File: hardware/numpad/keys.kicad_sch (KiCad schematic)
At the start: 30 parts, among them SW10 5, SW12 2, SW13 dot, SW14 times, SW15 9, SW16 6, SW17 3, SW18 minus, SW19 plus, SW2 Num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

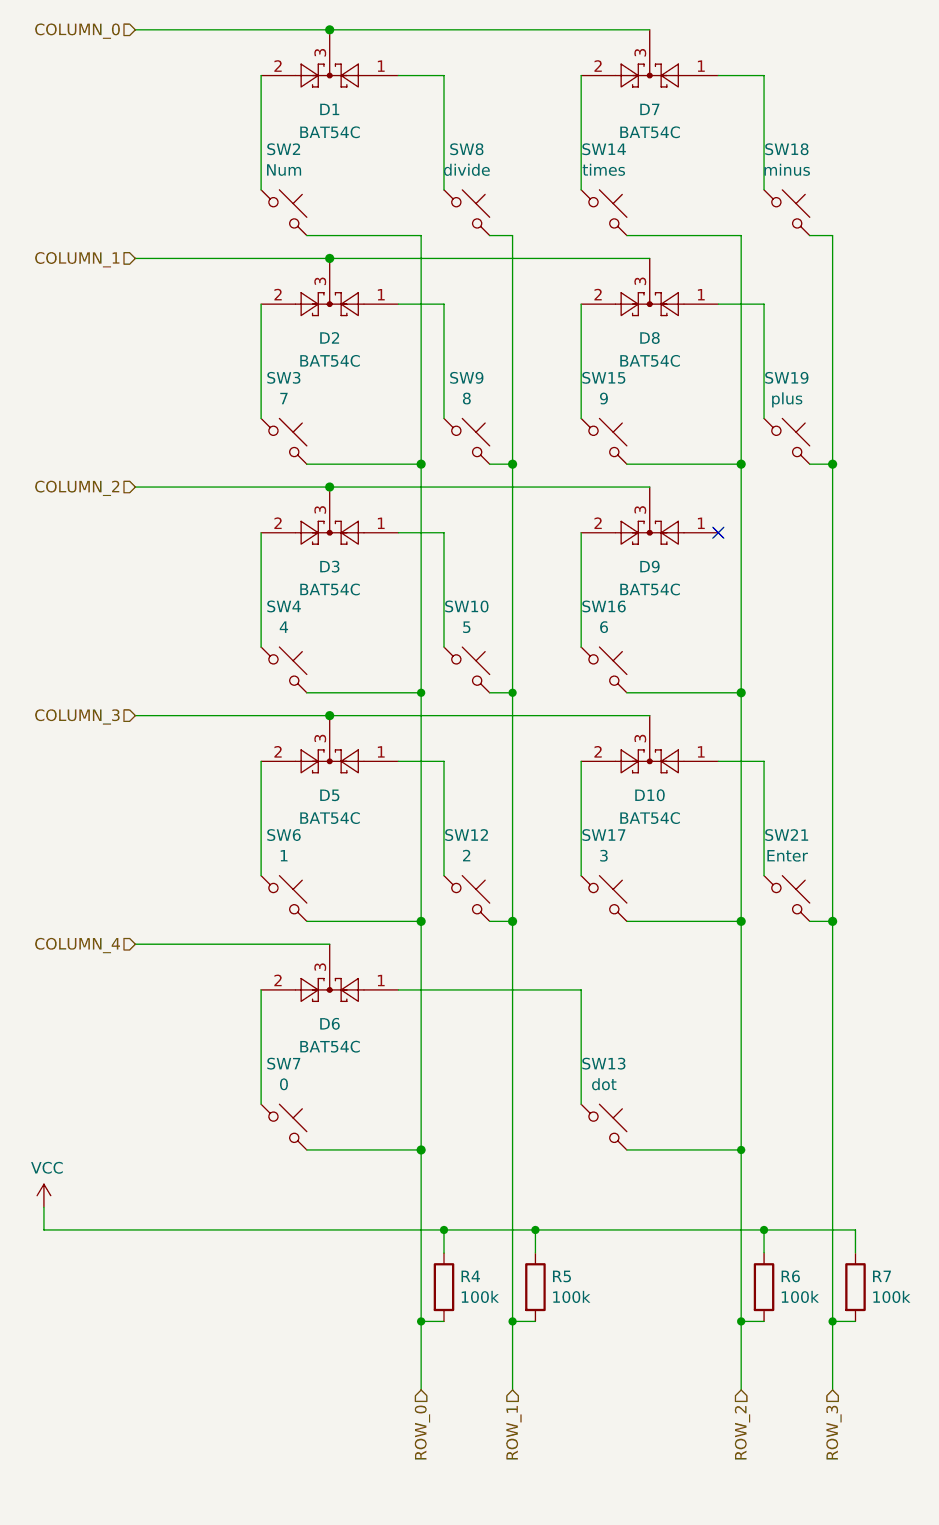
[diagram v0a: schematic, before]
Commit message: Numpad: Fix labels of columns and rows of the key matrix
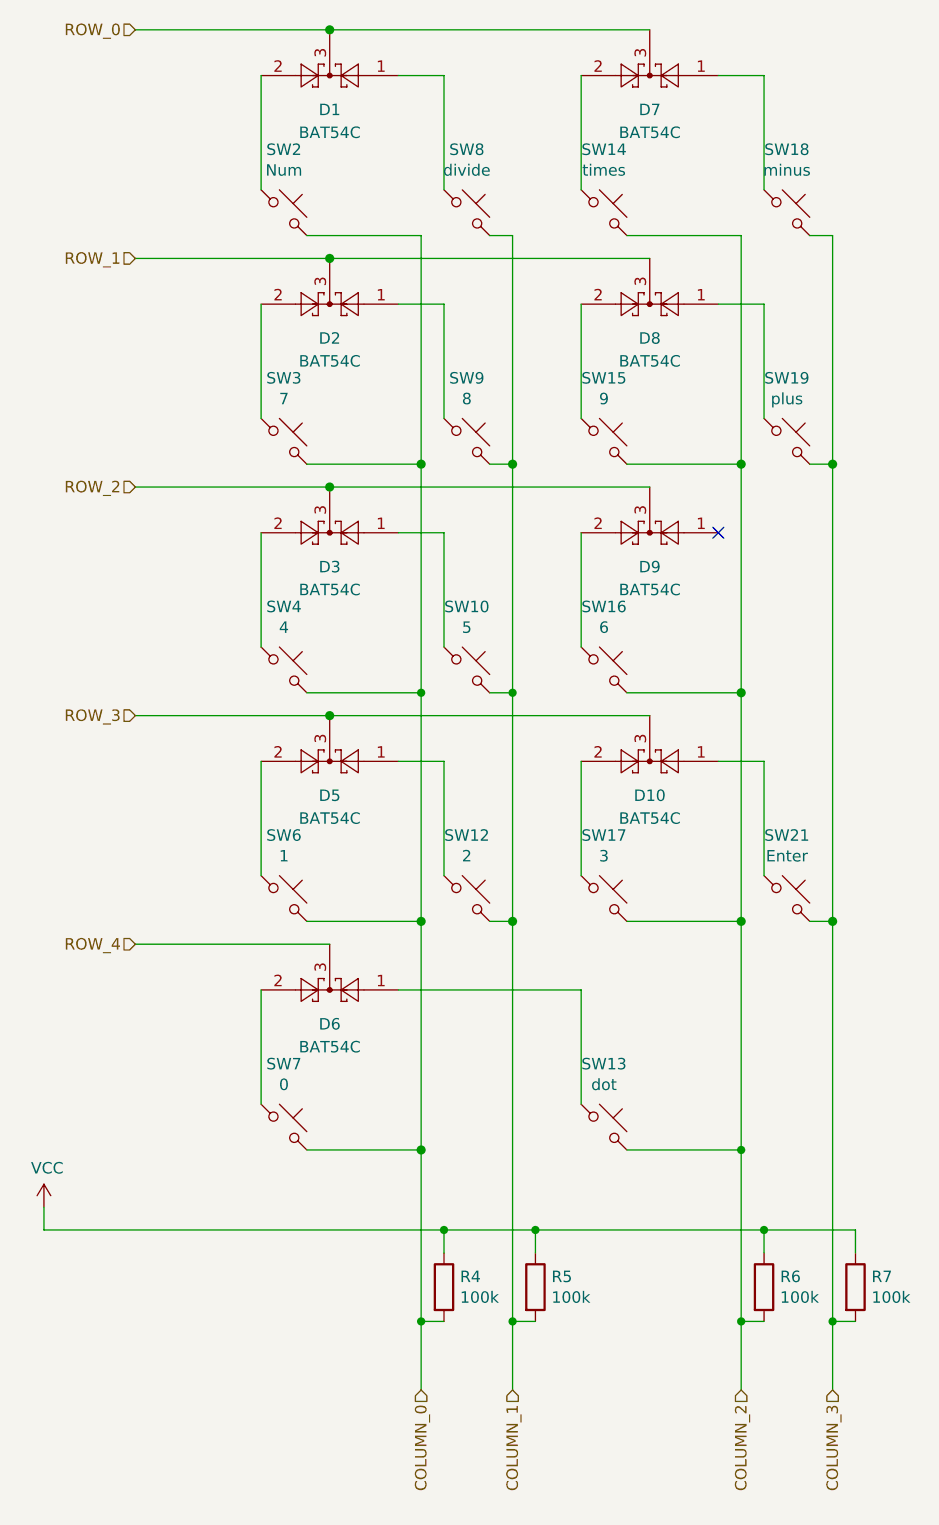
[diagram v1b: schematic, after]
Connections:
- net COLUMN_0: now also R4.2, SW2.2, SW3.2, SW4.2, SW6.2, SW7.2; no longer D1.3, D7.3
- net COLUMN_1: now also R5.2, SW10.2, SW12.2, SW8.2, SW9.2; no longer D2.3, D8.3
- net COLUMN_2: now also R6.2, SW13.2, SW14.2, SW15.2, SW16.2, SW17.2; no longer D3.3, D9.3
- net COLUMN_3: now also R7.2, SW18.2, SW19.2, SW21.2; no longer D10.3, D5.3
- net ROW_0: now also D1.3, D7.3; no longer R4.2, SW2.2, SW3.2, SW4.2, SW6.2, SW7.2
- net ROW_1: now also D2.3, D8.3; no longer R5.2, SW10.2, SW12.2, SW8.2, SW9.2
- net ROW_2: now also D3.3, D9.3; no longer R6.2, SW13.2, SW14.2, SW15.2, SW16.2, SW17.2
- net ROW_3: now also D10.3, D5.3; no longer R7.2, SW18.2, SW19.2, SW21.2
- net COLUMN_4 renamed ROW_4
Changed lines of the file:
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@@
     (stroke (width 0) (type solid) (color 0 0 0 0))
   )
-  (hierarchical_label "COLUMN_0" (shape input) (at 81.28 27.94 180)
+  (hierarchical_label "ROW_0" (shape input) (at 81.28 27.94 180)
     (effects (font (size 1.27 1.27)) (justify right))
   )
-  (hierarchical_label "COLUMN_1" (shape input) (at 81.28 53.34 180)
+  (hierarchical_label "ROW_1" (shape input) (at 81.28 53.34 180)
     (effects (font (size 1.27 1.27)) (justify right))
   )
-  (hierarchical_label "COLUMN_2" (shape input) (at 81.28 78.74 180)
+  (hierarchical_label "ROW_2" (shape input) (at 81.28 78.74 180)
     (effects (font (size 1.27 1.27)) (justify right))
   )
-  (hierarchical_label "COLUMN_3" (shape input) (at 81.28 104.14 180)
+  (hierarchical_label "ROW_3" (shape input) (at 81.28 104.14 180)
     (effects (font (size 1.27 1.27)) (justify right))
   )
-  (hierarchical_label "COLUMN_4" (shape input) (at 81.28 129.54 180)
+  (hierarchical_label "ROW_4" (shape input) (at 81.28 129.54 180)
     (effects (font (size 1.27 1.27)) (justify right))
   )
-  (hierarchical_label "ROW_0" (shape input) (at 113.03 179.07 270)
+  (hierarchical_label "COLUMN_0" (shape input) (at 113.03 179.07 270)
     (effects (font (size 1.27 1.27)) (justify right))
   )
-  (hierarchical_label "ROW_1" (shape input) (at 123.19 179.07 270)
+  (hierarchical_label "COLUMN_1" (shape input) (at 123.19 179.07 270)
     (effects (font (size 1.27 1.27)) (justify right))
   )
-  (hierarchical_label "ROW_2" (shape input) (at 148.59 179.07 270)
+  (hierarchical_label "COLUMN_2" (shape input) (at 148.59 179.07 270)
     (effects (font (size 1.27 1.27)) (justify right))
   )
-  (hierarchical_label "ROW_3" (shape input) (at 158.75 179.07 270)
+  (hierarchical_label "COLUMN_3" (shape input) (at 158.75 179.07 270)
     (effects (font (size 1.27 1.27)) (justify right))
   )

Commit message: Numpad: Add missing part numbers
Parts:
- SW10, SW12, SW13, SW14, SW15, SW16, SW17, SW18, SW19, SW2, SW21, SW3, SW4, SW6, SW7, SW8, SW9: Mouser (none) -> 540-MX1A-E1NW; Part Name (none) -> MX1A-E1NW
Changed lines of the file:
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@@
+      (effects (font (size 1.27 1.27)) hide)
+    )
+    (property "Mouser" "540-MX1A-E1NW" (id 4) (at 97.79 48.26 0)
+      (effects (font (size 1.27 1.27)) hide)
+    )
+    (property "Part Name" "MX1A-E1NW" (id 5) (at 97.79 48.26 0)
       (effects (font (size 1.27 1.27)) hide)
     )
@@
       (effects (font (size 1.27 1.27)) hide)
     )
+    (property "Mouser" "540-MX1A-E1NW" (id 4) (at 97.79 73.66 0)
+      (effects (font (size 1.27 1.27)) hide)
+    )
+    (property "Part Name" "MX1A-E1NW" (id 5) (at 97.79 73.66 0)
+      (effects (font (size 1.27 1.27)) hide)
+    )
     (pin "1")
     (pin "2")
@@
       (effects (font (size 1.27 1.27)) hide)
     )
+    (property "Mouser" "540-MX1A-E1NW" (id 4) (at 97.79 99.06 0)
+      (effects (font (size 1.27 1.27)) hide)
+    )
+    (property "Part Name" "MX1A-E1NW" (id 5) (at 97.79 99.06 0)
+      (effects (font (size 1.27 1.27)) hide)
+    )
     (pin "1")
     (pin "2")
@@
       (effects (font (size 1.27 1.27)) hide)
     )
+    (property "Mouser" "540-MX1A-E1NW" (id 4) (at 97.79 124.46 0)
+      (effects (font (size 1.27 1.27)) hide)
+    )
+    (property "Part Name" "MX1A-E1NW" (id 5) (at 97.79 124.46 0)
+      (effects (font (size 1.27 1.27)) hide)
+    )
     (pin "1")
     (pin "2")
@@
       (effects (font (size 1.27 1.27)) hide)
     )
+    (property "Mouser" "540-MX1A-E1NW" (id 4) (at 97.79 149.86 0)
+      (effects (font (size 1.27 1.27)) hide)
+    )
+    (property "Part Name" "MX1A-E1NW" (id 5) (at 97.79 149.86 0)
+      (effects (font (size 1.27 1.27)) hide)
+    )
     (pin "1")
     (pin "2")
@@
       (effects (font (size 1.27 1.27)) hide)
     )
+    (property "Mouser" "540-MX1A-E1NW" (id 4) (at 118.11 48.26 0)
+      (effects (font (size 1.27 1.27)) hide)
+    )
+    (property "Part Name" "MX1A-E1NW" (id 5) (at 118.11 48.26 0)
+      (effects (font (size 1.27 1.27)) hide)
+    )
     (pin "1")
     (pin "2")
@@
       (effects (font (size 1.27 1.27)) hide)
     )
+    (property "Mouser" "540-MX1A-E1NW" (id 4) (at 118.11 73.66 0)
+      (effects (font (size 1.27 1.27)) hide)
+    )
+    (property "Part Name" "MX1A-E1NW" (id 5) (at 118.11 73.66 0)
+      (effects (font (size 1.27 1.27)) hide)
+    )
     (pin "1")
     (pin "2")
@@
       (effects (font (size 1.27 1.27)) hide)
     )
+    (property "Mouser" "540-MX1A-E1NW" (id 4) (at 118.11 99.06 0)
+      (effects (font (size 1.27 1.27)) hide)
+    )
+    (property "Part Name" "MX1A-E1NW" (id 5) (at 118.11 99.06 0)
+      (effects (font (size 1.27 1.27)) hide)
+    )
     (pin "1")
     (pin "2")
@@
       (effects (font (size 1.27 1.27)) hide)
     )
+    (property "Mouser" "540-MX1A-E1NW" (id 4) (at 118.11 124.46 0)
+      (effects (font (size 1.27 1.27)) hide)
+    )
+    (property "Part Name" "MX1A-E1NW" (id 5) (at 118.11 124.46 0)
+      (effects (font (size 1.27 1.27)) hide)
+    )
     (pin "1")
     (pin "2")
@@
       (effects (font (size 1.27 1.27)) hide)
     )
+    (property "Mouser" "540-MX1A-E1NW" (id 4) (at 133.35 48.26 0)
+      (effects (font (size 1.27 1.27)) hide)
+    )
+    (property "Part Name" "MX1A-E1NW" (id 5) (at 133.35 48.26 0)
+      (effects (font (size 1.27 1.27)) hide)
+    )
     (pin "1")
     (pin "2")
@@
       (effects (font (size 1.27 1.27)) hide)
     )
+    (property "Mouser" "540-MX1A-E1NW" (id 4) (at 133.35 73.66 0)
+      (effects (font (size 1.27 1.27)) hide)
+    )
+    (property "Part Name" "MX1A-E1NW" (id 5) (at 133.35 73.66 0)
+      (effects (font (size 1.27 1.27)) hide)
+    )
     (pin "1")
     (pin "2")
@@
       (effects (font (size 1.27 1.27)) hide)
     )
+    (property "Mouser" "540-MX1A-E1NW" (id 4) (at 133.35 99.06 0)
+      (effects (font (size 1.27 1.27)) hide)
+    )
+    (property "Part Name" "MX1A-E1NW" (id 5) (at 133.35 99.06 0)
+      (effects (font (size 1.27 1.27)) hide)
+    )
     (pin "1")
     (pin "2")
@@
       (effects (font (size 1.27 1.27)) hide)
     )
+    (property "Mouser" "540-MX1A-E1NW" (id 4) (at 133.35 124.46 0)
+      (effects (font (size 1.27 1.27)) hide)
+    )
+    (property "Part Name" "MX1A-E1NW" (id 5) (at 133.35 124.46 0)
+      (effects (font (size 1.27 1.27)) hide)
+    )
     (pin "1")
     (pin "2")
@@
       (effects (font (size 1.27 1.27)) hide)
     )
+    (property "Mouser" "540-MX1A-E1NW" (id 4) (at 133.35 149.86 0)
+      (effects (font (size 1.27 1.27)) hide)
+    )
+    (property "Part Name" "MX1A-E1NW" (id 5) (at 133.35 149.86 0)
+      (effects (font (size 1.27 1.27)) hide)
+    )
     (pin "1")
     (pin "2")
@@
       (effects (font (size 1.27 1.27)) hide)
     )
+    (property "Mouser" "540-MX1A-E1NW" (id 4) (at 153.67 48.26 0)
+      (effects (font (size 1.27 1.27)) hide)
+    )
+    (property "Part Name" "MX1A-E1NW" (id 5) (at 153.67 48.26 0)
+      (effects (font (size 1.27 1.27)) hide)
+    )
     (pin "1")
     (pin "2")
@@
       (effects (font (size 1.27 1.27)) hide)
     )
+    (property "Mouser" "540-MX1A-E1NW" (id 4) (at 153.67 73.66 0)
+      (effects (font (size 1.27 1.27)) hide)
+    )
+    (property "Part Name" "MX1A-E1NW" (id 5) (at 153.67 73.66 0)
+      (effects (font (size 1.27 1.27)) hide)
+    )
     (pin "1")
     (pin "2")
@@
       (effects (font (size 1.27 1.27)) hide)
     )
+    (property "Mouser" "540-MX1A-E1NW" (id 4) (at 153.67 124.46 0)
+      (effects (font (size 1.27 1.27)) hide)
+    )
+    (property "Part Name" "MX1A-E1NW" (id 5) (at 153.67 124.46 0)
+      (effects (font (size 1.27 1.27)) hide)
+    )

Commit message: Numpad: Add pullup for reset and connect BOOT0 to ground
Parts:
- D1, D10, D2, D3, D5, D6, D7, D8, D9: Mouser 241-BAT54A_R1_00001 -> 241-BAT54A_R1_00001
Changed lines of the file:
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@@
       (effects (font (size 1.27 1.27)) hide)
     )
-    (property "Mouser" " 241-BAT54A_R1_00001 " (id 5) (at 102.87 33.02 0)
+    (property "Mouser" "241-BAT54A_R1_00001 " (id 5) (at 102.87 33.02 0)
       (effects (font (size 1.27 1.27)) hide)
     )
@@
       (effects (font (size 1.27 1.27)) hide)
     )
-    (property "Mouser" " 241-BAT54A_R1_00001 " (id 5) (at 102.87 58.42 0)
+    (property "Mouser" "241-BAT54A_R1_00001 " (id 5) (at 102.87 58.42 0)
       (effects (font (size 1.27 1.27)) hide)
     )
@@
       (effects (font (size 1.27 1.27)) hide)
     )
-    (property "Mouser" " 241-BAT54A_R1_00001 " (id 5) (at 102.87 83.82 0)
+    (property "Mouser" "241-BAT54A_R1_00001 " (id 5) (at 102.87 83.82 0)
       (effects (font (size 1.27 1.27)) hide)
     )
@@
       (effects (font (size 1.27 1.27)) hide)
     )
-    (property "Mouser" " 241-BAT54A_R1_00001 " (id 5) (at 102.87 109.22 0)
+    (property "Mouser" "241-BAT54A_R1_00001 " (id 5) (at 102.87 109.22 0)
       (effects (font (size 1.27 1.27)) hide)
     )
@@
       (effects (font (size 1.27 1.27)) hide)
     )
-    (property "Mouser" " 241-BAT54A_R1_00001 " (id 5) (at 102.87 134.62 0)
+    (property "Mouser" "241-BAT54A_R1_00001 " (id 5) (at 102.87 134.62 0)
       (effects (font (size 1.27 1.27)) hide)
     )
@@
       (effects (font (size 1.27 1.27)) hide)
     )
-    (property "Mouser" " 241-BAT54A_R1_00001 " (id 5) (at 138.43 33.02 0)
+    (property "Mouser" "241-BAT54A_R1_00001 " (id 5) (at 138.43 33.02 0)
       (effects (font (size 1.27 1.27)) hide)
     )
@@
       (effects (font (size 1.27 1.27)) hide)
     )
-    (property "Mouser" " 241-BAT54A_R1_00001 " (id 5) (at 138.43 58.42 0)
+    (property "Mouser" "241-BAT54A_R1_00001 " (id 5) (at 138.43 58.42 0)
       (effects (font (size 1.27 1.27)) hide)
     )
@@
       (effects (font (size 1.27 1.27)) hide)
     )
-    (property "Mouser" " 241-BAT54A_R1_00001 " (id 5) (at 138.43 83.82 0)
+    (property "Mouser" "241-BAT54A_R1_00001 " (id 5) (at 138.43 83.82 0)
       (effects (font (size 1.27 1.27)) hide)
     )
@@
       (effects (font (size 1.27 1.27)) hide)
     )
-    (property "Mouser" " 241-BAT54A_R1_00001 " (id 5) (at 138.43 109.22 0)
+    (property "Mouser" "241-BAT54A_R1_00001 " (id 5) (at 138.43 109.22 0)
       (effects (font (size 1.27 1.27)) hide)
     )

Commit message: Numpad: Add mounting holes
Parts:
- D1, D10, D2, D3, D5, D6, D7, D8, D9: Mouser 241-BAT54A_R1_00001 -> 241-BAT54C_R1_00001; Part Name BAT54A -> BAT54C
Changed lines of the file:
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@@
       (effects (font (size 1.27 1.27)) hide)
     )
-    (property "Part Name" "BAT54A" (id 4) (at 102.87 33.02 0)
+    (property "Part Name" "BAT54C" (id 4) (at 102.87 33.02 0)
       (effects (font (size 1.27 1.27)) hide)
     )
-    (property "Mouser" "241-BAT54A_R1_00001 " (id 5) (at 102.87 33.02 0)
+    (property "Mouser" "241-BAT54C_R1_00001 " (id 5) (at 102.87 33.02 0)
       (effects (font (size 1.27 1.27)) hide)
     )
@@
       (effects (font (size 1.27 1.27)) hide)
     )
-    (property "Part Name" "BAT54A" (id 4) (at 102.87 58.42 0)
+    (property "Part Name" "BAT54C" (id 4) (at 102.87 58.42 0)
       (effects (font (size 1.27 1.27)) hide)
     )
-    (property "Mouser" "241-BAT54A_R1_00001 " (id 5) (at 102.87 58.42 0)
+    (property "Mouser" "241-BAT54C_R1_00001 " (id 5) (at 102.87 58.42 0)
       (effects (font (size 1.27 1.27)) hide)
     )
@@
       (effects (font (size 1.27 1.27)) hide)
     )
-    (property "Part Name" "BAT54A" (id 4) (at 102.87 83.82 0)
+    (property "Part Name" "BAT54C" (id 4) (at 102.87 83.82 0)
       (effects (font (size 1.27 1.27)) hide)
     )
-    (property "Mouser" "241-BAT54A_R1_00001 " (id 5) (at 102.87 83.82 0)
+    (property "Mouser" "241-BAT54C_R1_00001 " (id 5) (at 102.87 83.82 0)
       (effects (font (size 1.27 1.27)) hide)
     )
@@
       (effects (font (size 1.27 1.27)) hide)
     )
-    (property "Part Name" "BAT54A" (id 4) (at 102.87 109.22 0)
+    (property "Part Name" "BAT54C" (id 4) (at 102.87 109.22 0)
       (effects (font (size 1.27 1.27)) hide)
     )
-    (property "Mouser" "241-BAT54A_R1_00001 " (id 5) (at 102.87 109.22 0)
+    (property "Mouser" "241-BAT54C_R1_00001 " (id 5) (at 102.87 109.22 0)
       (effects (font (size 1.27 1.27)) hide)
     )
@@
       (effects (font (size 1.27 1.27)) hide)
     )
-    (property "Part Name" "BAT54A" (id 4) (at 102.87 134.62 0)
+    (property "Part Name" "BAT54C" (id 4) (at 102.87 134.62 0)
       (effects (font (size 1.27 1.27)) hide)
     )
-    (property "Mouser" "241-BAT54A_R1_00001 " (id 5) (at 102.87 134.62 0)
+    (property "Mouser" "241-BAT54C_R1_00001 " (id 5) (at 102.87 134.62 0)
       (effects (font (size 1.27 1.27)) hide)
     )
@@
       (effects (font (size 1.27 1.27)) hide)
     )
-    (property "Part Name" "BAT54A" (id 4) (at 138.43 33.02 0)
+    (property "Part Name" "BAT54C" (id 4) (at 138.43 33.02 0)
       (effects (font (size 1.27 1.27)) hide)
     )
-    (property "Mouser" "241-BAT54A_R1_00001 " (id 5) (at 138.43 33.02 0)
+    (property "Mouser" "241-BAT54C_R1_00001 " (id 5) (at 138.43 33.02 0)
       (effects (font (size 1.27 1.27)) hide)
     )
@@
       (effects (font (size 1.27 1.27)) hide)
     )
-    (property "Part Name" "BAT54A" (id 4) (at 138.43 58.42 0)
+    (property "Part Name" "BAT54C" (id 4) (at 138.43 58.42 0)
       (effects (font (size 1.27 1.27)) hide)
     )
-    (property "Mouser" "241-BAT54A_R1_00001 " (id 5) (at 138.43 58.42 0)
+    (property "Mouser" "241-BAT54C_R1_00001 " (id 5) (at 138.43 58.42 0)
       (effects (font (size 1.27 1.27)) hide)
     )
@@
       (effects (font (size 1.27 1.27)) hide)
     )
-    (property "Part Name" "BAT54A" (id 4) (at 138.43 83.82 0)
+    (property "Part Name" "BAT54C" (id 4) (at 138.43 83.82 0)
       (effects (font (size 1.27 1.27)) hide)
     )
-    (property "Mouser" "241-BAT54A_R1_00001 " (id 5) (at 138.43 83.82 0)
+    (property "Mouser" "241-BAT54C_R1_00001 " (id 5) (at 138.43 83.82 0)
       (effects (font (size 1.27 1.27)) hide)
     )
@@
       (effects (font (size 1.27 1.27)) hide)
     )
-    (property "Part Name" "BAT54A" (id 4) (at 138.43 109.22 0)
+    (property "Part Name" "BAT54C" (id 4) (at 138.43 109.22 0)
       (effects (font (size 1.27 1.27)) hide)
     )
-    (property "Mouser" "241-BAT54A_R1_00001 " (id 5) (at 138.43 109.22 0)
+    (property "Mouser" "241-BAT54C_R1_00001 " (id 5) (at 138.43 109.22 0)
       (effects (font (size 1.27 1.27)) hide)
     )
